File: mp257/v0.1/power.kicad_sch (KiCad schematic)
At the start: 129 parts, among them U1 STM32MP257FAK3, U26 STPMIC25APQR, U9 MCP1501-18xCH

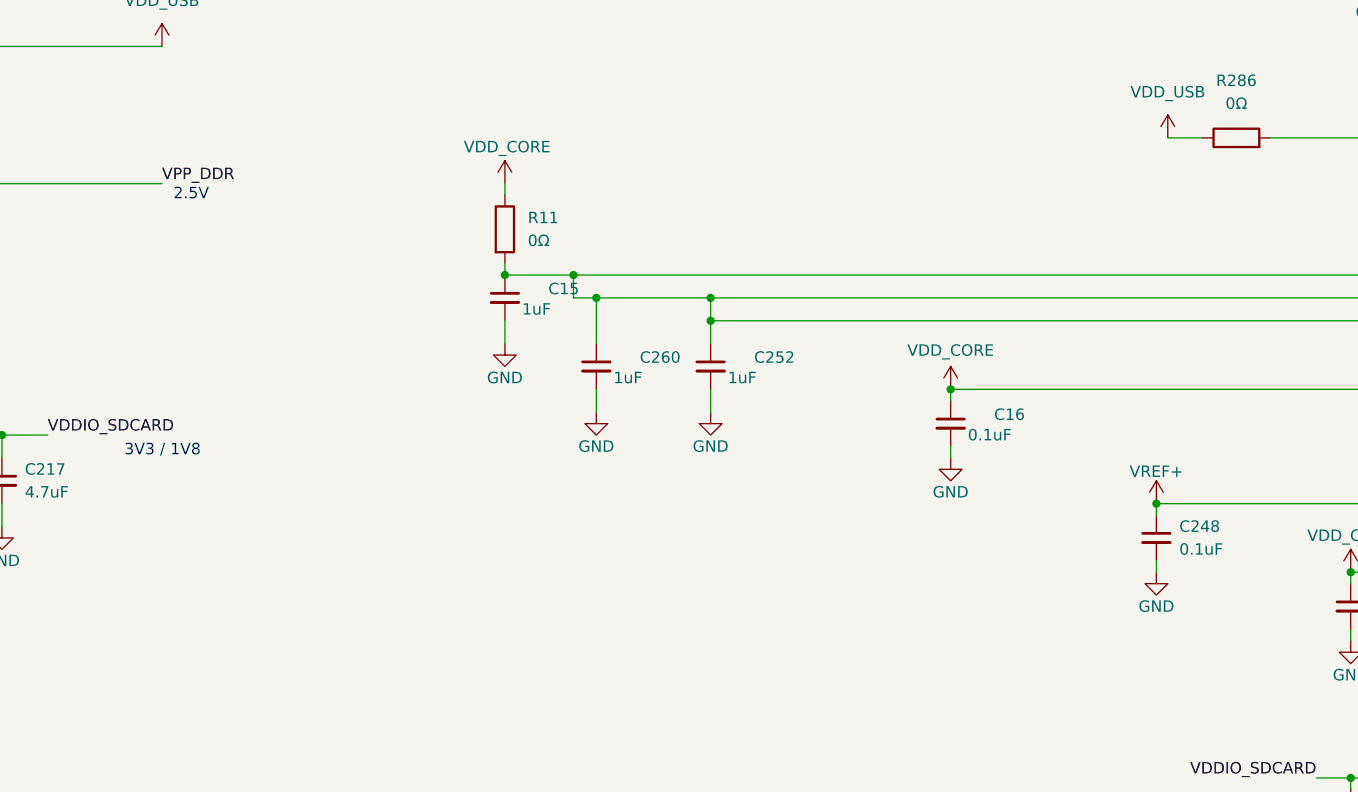
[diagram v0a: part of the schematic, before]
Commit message: pmic placement
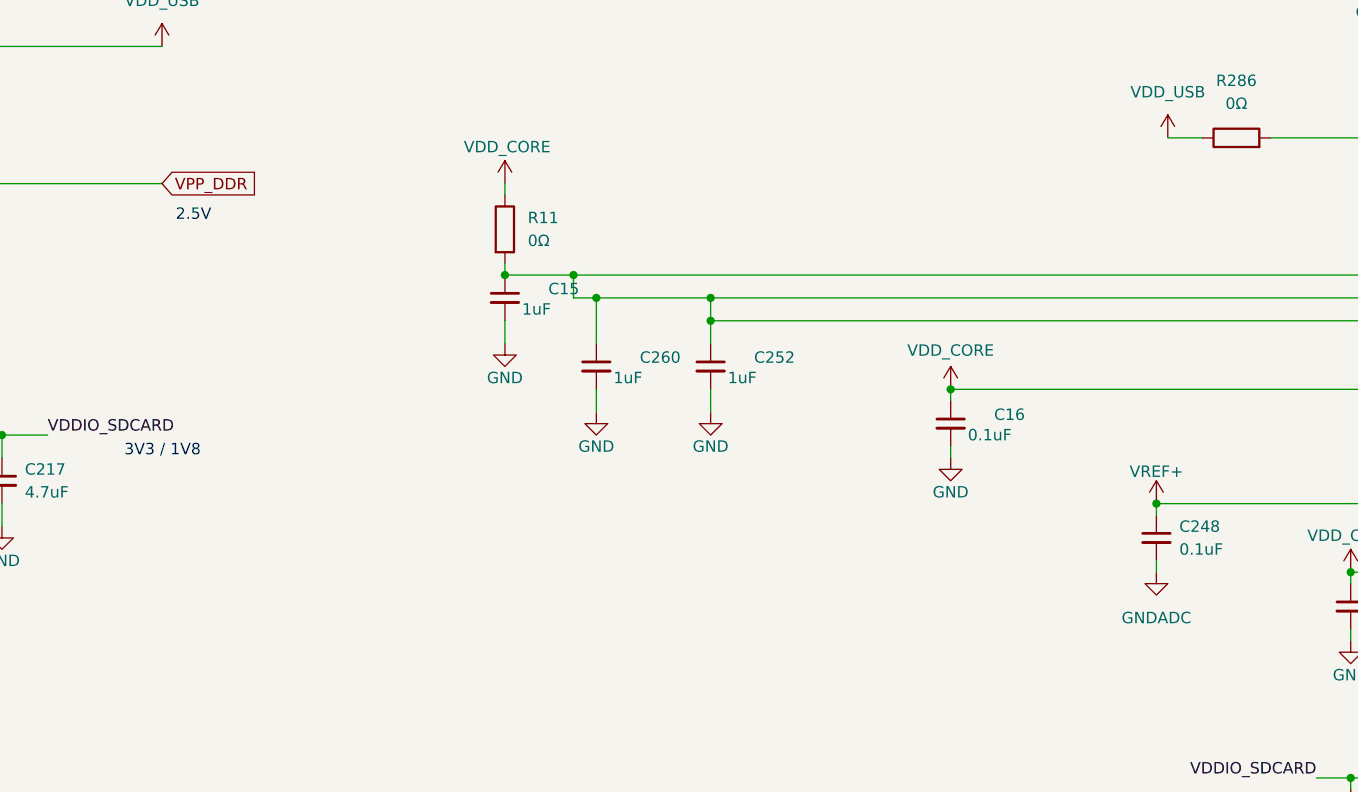
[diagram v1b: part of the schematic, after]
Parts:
- R11: footprint 4ms_Resistor:R_0603 -> 4ms_Resistor:R_0402; symbol 4ms_Resistor_0603:0Ω_0603 -> 4ms_Resistor_0402:0Ω_0402; JLCPCB ID C21189 -> C106231; Part Number RC0603FR-070RL -> RC0402FR-070RL; Specifications 0Ω, 1%, 1/10W, 0603 -> 0Ω, 1%, 1/16W, 0402
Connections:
- net GND: no longer C248.2
- net GNDADC: now also C248.2
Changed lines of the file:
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@@
 	(text "2.5V"
 		(exclude_from_sim no)
-		(at 269.24 247.142 0)
+		(at 269.494 249.428 0)
 		(effects
 			(font
@@
 		)
 	)
-	(label "VPP_DDR"
-		(at 267.97 245.11 0)
+	(label "VDDIO_SDCARD"
+		(at 396.24 311.15 180)
 		(effects
 			(font
 				(size 1.27 1.27)
 			)
-			(justify left bottom)
+			(justify right bottom)
 		)
 	)
-	(label "VDDIO_SDCARD"
-		(at 396.24 311.15 180)
+	(global_label "VPP_DDR"
+		(shape input)
+		(at 267.97 245.11 0)
+		(fields_autoplaced yes)
 		(effects
 			(font
 				(size 1.27 1.27)
 			)
-			(justify right bottom)
+			(justify left)
+		)
+		(property "Intersheetrefs" "${INTERSHEET_REFS}"
+			(at 279.3614 245.11 0)
+			(effects
+				(font
+					(size 1.27 1.27)
+				)
+				(justify left)
+				(hide yes)
+			)
 		)
 	)
@@
 	)
 	(symbol
-		(lib_id "power:GND")
-		(at 378.46 288.29 0)
-		(unit 1)
-		(exclude_from_sim no)
-		(in_bom yes)
-		(on_board yes)
-		(dnp no)
-		(property "Reference" "#PWR079"
-			(at 378.46 288.29 0)
-			(effects
-				(font
-					(size 1.27 1.27)
-				)
-				(hide yes)
-			)
-		)
-		(property "Value" "GND"
-			(at 378.46 292.1 0)
-			(effects
-				(font
-					(size 1.27 1.27)
-				)
-			)
-		)
-		(property "Footprint" ""
-			(at 378.46 288.29 0)
-			(effects
-				(font
-					(size 1.27 1.27)
-				)
-				(hide yes)
-			)
-		)
-		(property "Datasheet" ""
-			(at 378.46 288.29 0)
-			(effects
-				(font
-					(size 1.27 1.27)
-				)
-				(hide yes)
-			)
-		)
-		(property "Description" "Power symbol creates a global label with name \"GND\" , ground"
-			(at 378.46 288.29 0)
-			(effects
-				(font
-					(size 1.27 1.27)
-				)
-				(hide yes)
-			)
-		)
-		(pin "1"
-		)
-		(instances
-			(project "mp257-devboard"
-				(path "/64ec1a6b-f4f9-4414-abbd-a05816451f08/200f2e9a-f79b-4306-8e51-ebf831da81bb"
-					(reference "#PWR079")
-					(unit 1)
-				)
-			)
-		)
-	)
-	(symbol
 		(lib_id "4ms_Capacitor:22uF_0805_10V")
 		(at 191.77 161.29 0)
@@
 	)
 	(symbol
+		(lib_id "4ms_Power_Symbol:GNDADC")
+		(at 378.46 288.29 0)
+		(unit 1)
+		(exclude_from_sim no)
+		(in_bom yes)
+		(on_board yes)
+		(dnp no)
+		(fields_autoplaced yes)
+		(property "Reference" "#PWR079"
+			(at 378.46 294.64 0)
+			(effects
+				(font
+					(size 1.27 1.27)
+				)
+				(hide yes)
+			)
+		)
+		(property "Value" "GNDADC"
+			(at 378.46 293.37 0)
+			(effects
+				(font
+					(size 1.27 1.27)
+				)
+			)
+		)
+		(property "Footprint" ""
+			(at 378.46 288.29 0)
+			(effects
+				(font
+					(size 1.27 1.27)
+				)
+			)
+		)
+		(property "Datasheet" ""
+			(at 378.46 288.29 0)
+			(effects
+				(font
+					(size 1.27 1.27)
+				)
+			)
+		)
+		(property "Description" ""
+			(at 378.46 288.29 0)
+			(effects
+				(font
+					(size 1.27 1.27)
+				)
+				(hide yes)
+			)
+		)
+		(pin "1"
+		)
+		(instances
+			(project "mp257-devboard"
+				(path "/64ec1a6b-f4f9-4414-abbd-a05816451f08/200f2e9a-f79b-4306-8e51-ebf831da81bb"
+					(reference "#PWR079")
+					(unit 1)
+				)
+			)
+		)
+	)
+	(symbol
 		(lib_id "4ms_Capacitor:1uF_0402_25V")
 		(at 52.07 269.24 0)
@@
 	)
 	(symbol
-		(lib_id "4ms_Resistor_0603:0Ω_0603")
+		(lib_id "4ms_Resistor_0402:0Ω_0402")
 		(at 306.07 250.19 0)
 		(unit 1)
@@
 			)
 		)
-		(property "Footprint" "4ms_Resistor:R_0603"
+		(property "Footprint" "4ms_Resistor:R_0402"
 			(at 303.53 263.144 0)
 			(effects
@@
 			)
 		)
-		(property "Description" "0Ω, 1%, 1/10W, 0603"
+		(property "Description" "0Ω, 1%, 1/16W, 0402"
 			(at 306.07 250.19 0)
 			(effects
@@
 			)
 		)
-		(property "Specifications" "0Ω, 1%, 1/10W, 0603"
+		(property "Specifications" "0Ω, 1%, 1/16W, 0402"
 			(at 303.53 257.81 0)
 			(effects
@@
 			)
 		)
-		(property "Part Number" "RC0603FR-070RL"
+		(property "Part Number" "RC0402FR-070RL"
 			(at 303.53 261.366 0)
 			(effects
@@
 			)
 		)
-		(property "JLCPCB ID" "C21189"
+		(property "JLCPCB ID" "C106231"
 			(at 303.53 264.922 0)
 			(effects

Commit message: mp257 placement WIP
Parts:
- C1, C10, C11, C12, C13, C15, C16, C17, C192, C195, C196, C2, C201, C220, C234, C236, C237, C238, C239, C240, C244, C246, C248, C251, C252, C253, C260, C3, C4, C44, C45, C46, C47, C48, C49, C5, C50, C51, C52, C58, C59, C6, C64, C68, C69, C7, C70, C71, C72, C74, C75, C76, C77, C8, C82: footprint 4ms_Capacitor:C_0201 -> 4ms_Capacitor:C_0201_TightCourtyard

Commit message: Routing...
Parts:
- C234: footprint 4ms_Capacitor:C_0201_TightCourtyard -> 4ms_Capacitor:C_0402; symbol 4ms_Capacitor:100nF_0201_16V -> 4ms_Capacitor:100nF_0402_16V; JLCPCB ID C711071 -> C1525; Part Number GRT033C81E104KE01D -> GCM155R71C104KA55D; Part Number 2 CC0201MRX5R6BB104 -> CC0402KRX7R7BB104; Specifications 0.1uF, Min. 16V 10%, X7R or X5R or X6S or similar -> 0.1uF, Min. 16V 10%, X7R or X5R or similar
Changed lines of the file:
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@@
 	)
 	(symbol
-		(lib_id "4ms_Capacitor:100nF_0201_16V")
+		(lib_id "4ms_Capacitor:100nF_0402_16V")
 		(at 524.51 327.66 0)
 		(unit 1)
@@
 			)
 		)
-		(property "Footprint" "4ms_Capacitor:C_0201_TightCourtyard"
+		(property "Footprint" "4ms_Capacitor:C_0402"
 			(at 521.97 332.74 0)
 			(effects
@@
 			)
 		)
-		(property "Description" "0.1uF, 0201, Min. 16V 10%, X7R or X5R or X6S or similar"
+		(property "Description" "0.1uF, Min. 16V 10%, X7R or X5R or similar"
 			(at 524.51 327.66 0)
 			(effects
@@
 			)
 		)
-		(property "Specifications" "0.1uF, Min. 16V 10%, X7R or X5R or X6S or similar"
+		(property "Specifications" "0.1uF, Min. 16V 10%, X7R or X5R or similar"
 			(at 521.97 335.534 0)
 			(effects
@@
 			)
 		)
-		(property "Part Number" "GRT033C81E104KE01D"
+		(property "Part Number" "GCM155R71C104KA55D"
 			(at 521.97 338.582 0)
 			(effects
@@
 			)
 		)
-		(property "JLCPCB ID" "C711071"
+		(property "JLCPCB ID" "C1525"
 			(at 525.78 340.36 0)
 			(effects
@@
 			)
 		)
-		(property "Part Number 2" "CC0201MRX5R6BB104"
+		(property "Part Number 2" "CC0402KRX7R7BB104"
 			(at 532.13 344.17 0)
 			(effects

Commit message: Silk cleanup, final routing
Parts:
- removed C207: 22uF_0805_10V, 4ms_Capacitor:C_0805, symbol 4ms_Capacitor:22uF_0805_10V
- removed C34: 22uF_0603_6.3V, 4ms_Capacitor:C_0603, symbol 4ms_Capacitor:22uF_0603_6.3V
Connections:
- net +5V: no longer C42.1, U9.4 (~{SHDN}), U9.6 (VDD)
- net VDD_IO: now also C42.1, U9.4 (~{SHDN}), U9.6 (VDD)

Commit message: Cleanup BOM, update all parts from lib
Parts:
- C225, C235: footprint 4ms_Capacitor:C_0201 -> 4ms_Capacitor:C_0201_TightCourtyard
- C234: value 100nF_0201_16V -> 100nF_0402_16V
- R11: value 0Ω_0603 -> 0Ω_0402
- U1: ALTIUM_VALUE STM32MP257FAK3 -> (none); COMPONENTLINK1URL http://tunmcdsvn.tun.st.com/Component_Documentation_Library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 -> (none); COMPONENT_COUNTRY_OF_ORIGIN Unknown -> (none); ID 5491 -> (none); INTERNAL_PART_NUMBER MCD-03375 -> (none); MANUFACTURER STMICROELECTRONICS -> (none); MANUFACTURER_PART_NUMBER STM32MP257FAK3 -> (none); Manufacturer (none) -> STMICROELECTRONICS; ORDER_CODE_DIGIKEY N/A -> (none); ORDER_CODE_FARNELL N/A -> (none); ORDER_CODE_RS N/A -> (none); PACKAGE TFBGA -> (none); PART_PREFERENCE Recommended -> (none); PART_TYPE IC -> (none); Part Number (none) -> STM32MP257FAK3; SHOWFIELDS YES -> (none); STATUS Checked -> (none); Specifications (none) -> STM32MP257FAK3 MPU

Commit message: Fixing missing M P/N
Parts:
- C225: footprint 4ms_Capacitor:C_0201_TightCourtyard -> 4ms_Capacitor:C_0201; JLCPCB ID (none) -> C335103; Manufacturer (none) -> Murata; Part Number (none) -> GRM035R60J475ME15D
- C235: footprint 4ms_Capacitor:C_0201_TightCourtyard -> 4ms_Capacitor:C_0201; JLCPCB ID (none) -> C319184; Manufacturer (none) -> Murata; Part Number (none) -> GRM033R61A225ME47D
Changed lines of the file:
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@@
 			)
 		)
-		(property "Footprint" "4ms_Capacitor:C_0201_TightCourtyard"
+		(property "Footprint" "4ms_Capacitor:C_0201"
 			(at 415.29 229.87 0)
 			(effects
@@
 			)
 		)
-		(property "Manufacturer" ""
+		(property "Manufacturer" "Murata"
 			(at 419.1 238.76 0)
 			(effects
@@
 			)
 		)
-		(property "Part Number" ""
+		(property "Part Number" "GRM035R60J475ME15D"
 			(at 425.45 241.3 0)
 			(effects
@@
 			)
 		)
-		(property "JLCPCB ID" ""
+		(property "JLCPCB ID" "C335103"
 			(at 419.1 237.49 0)
 			(effects
@@
 			)
 		)
-		(property "Note" ""
-			(at 417.83 224.79 0)
-			(effects
-				(font
-					(size 1.27 1.27)
-				)
-				(hide yes)
-			)
-		)
 		(pin "1"
 		)
@@
 			)
 		)
-		(property "Footprint" "4ms_Capacitor:C_0201_TightCourtyard"
+		(property "Footprint" "4ms_Capacitor:C_0201"
 			(at 558.8 251.46 0)
 			(effects
@@
 			)
 		)
-		(property "Manufacturer" ""
+		(property "Manufacturer" "Murata"
 			(at 562.61 260.35 0)
 			(effects
@@
 			)
 		)
-		(property "Part Number" ""
+		(property "Part Number" "GRM033R61A225ME47D"
 			(at 568.96 262.89 0)
 			(effects
@@
 			)
 		)
-		(property "JLCPCB ID" ""
+		(property "JLCPCB ID" "C319184"
 			(at 562.61 259.08 0)
 			(effects
@@
 				(hide yes)
 			)
-		)
-		(property "Note" ""
-			(at 561.34 246.38 0)
-			(effects
-				(font
-					(size 1.27 1.27)
-				)
-				(hide yes)
-			)

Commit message: Missing p/n
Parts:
- C39, C40, C53: JLCPCB ID (none) -> C77000; Manufacturer (none) -> Murata; Part Number (none) -> GRM155R61A106ME44D
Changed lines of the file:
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@@
 			)
 		)
-		(property "Manufacturer" ""
+		(property "Manufacturer" "Murata"
 			(at 473.71 60.198 0)
 			(effects
@@
 			)
 		)
-		(property "Part Number" ""
+		(property "Part Number" "GRM155R61A106ME44D"
 			(at 473.71 61.722 0)
 			(effects
@@
 			)
 		)
-		(property "JLCPCB ID" ""
+		(property "JLCPCB ID" "C77000"
 			(at 477.52 63.5 0)
 			(effects
@@
 			)
 		)
-		(property "Note" ""
-			(at 476.25 50.8 0)
-			(effects
-				(font
-					(size 1.27 1.27)
-				)
-				(hide yes)
-			)
-		)
 		(pin "1"
 		)
@@
 			)
 		)
-		(property "Manufacturer" ""
+		(property "Manufacturer" "Murata"
 			(at 205.232 214.63 0)
 			(effects
@@
 			)
 		)
-		(property "Part Number" ""
+		(property "Part Number" "GRM155R61A106ME44D"
 			(at 203.708 214.63 0)
 			(effects
@@
 			)
 		)
-		(property "JLCPCB ID" ""
+		(property "JLCPCB ID" "C77000"
 			(at 201.93 218.44 0)
 			(effects
@@
 			)
 		)
-		(property "Note" ""
-			(at 214.63 217.17 90)
-			(effects
-				(font
-					(size 1.27 1.27)
-				)
-				(hide yes)
-			)
-		)
 		(pin "1"
 		)
@@
 			)
 		)
-		(property "Manufacturer" ""
+		(property "Manufacturer" "Murata"
 			(at 52.07 206.502 0)
 			(effects
@@
 			)
 		)
-		(property "Part Number" ""
+		(property "Part Number" "GRM155R61A106ME44D"
 			(at 52.07 204.978 0)
 			(effects
@@
 			)
 		)
-		(property "JLCPCB ID" ""
+		(property "JLCPCB ID" "C77000"
 			(at 48.26 203.2 0)
 			(effects
@@
 				(hide yes)
 			)
-		)
-		(property "Note" ""
-			(at 49.53 215.9 0)
-			(effects
-				(font
-					(size 1.27 1.27)
-				)
-				(hide yes)
-			)
